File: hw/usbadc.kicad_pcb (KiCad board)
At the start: 4 copper layers, 100 x 60 mm, 253 parts, among them J1 Ext_Power, J10 BNC, J11 PEN_SEL, J12 PUDC_B/IN, J2 USB_C_Receptacle_USB2.0, J3 Jtag_Master, J4 JTAG, J5 GPIO2V5, J6 BNC, J7 BNC, J8 BNC, J9 Expansion, Q1 Si3477, Q2 Si3477, SW1 PROG_B, U1 TLV62569DDC, U10 LMH6882, U11 TSV992A, U12 OPA859xDSG, U13 OPA859xDSG, U14 MCP47CVB02-E_UN, U15 UTC2000, U16 74LVC1G32, U17 SN74LVC2T45DCUR, U2 TLV62569DDC, U3 TLV62569DDC, U4 FT240XS, U5 XC3S50A-VQ100, U6 AT25DF041B, U7 5P49V5925, U8 THS4522, U9 MAX19507, Y1 25MHz

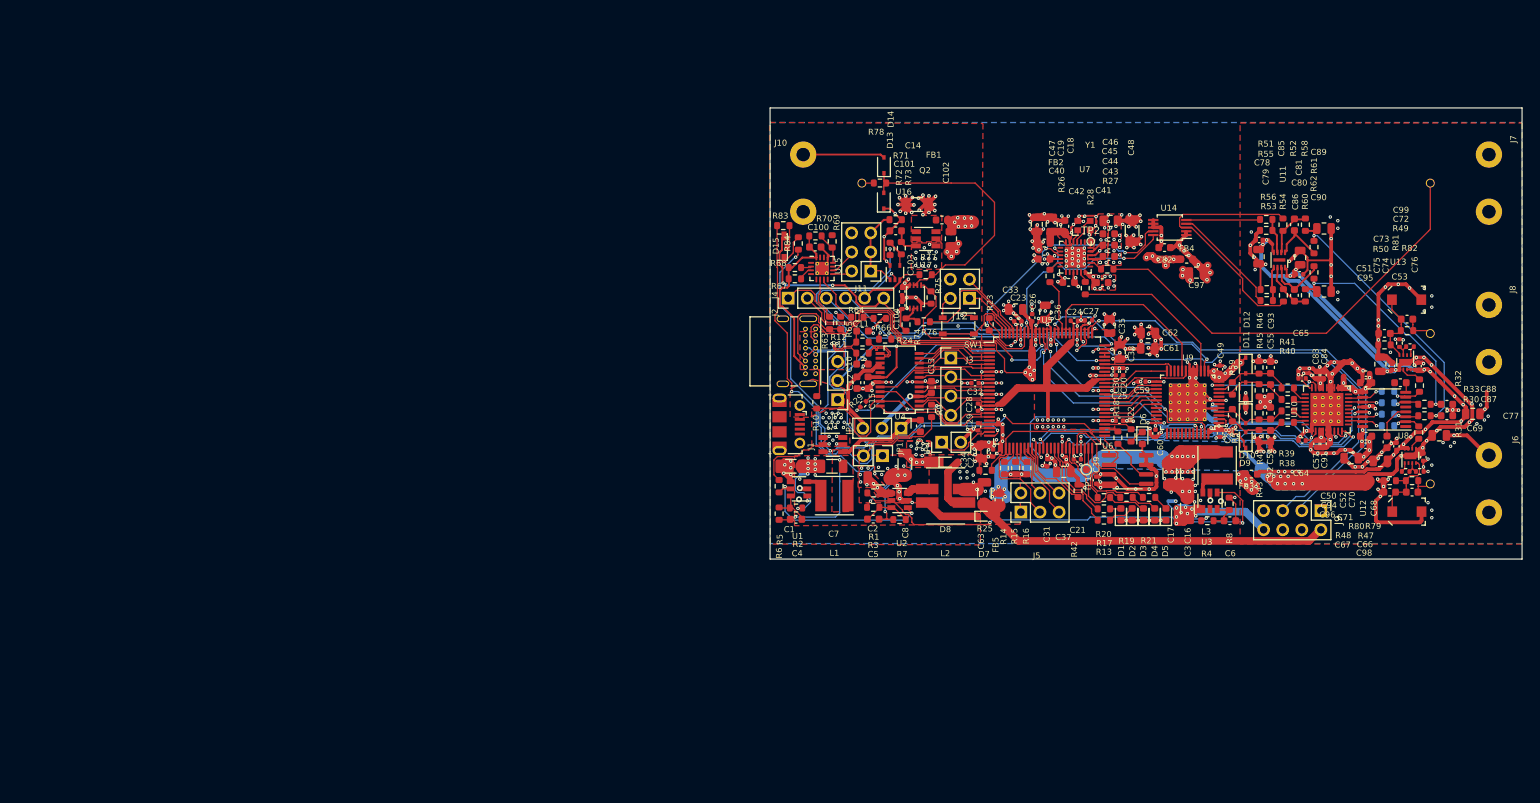
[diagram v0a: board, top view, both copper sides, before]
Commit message: basic schematic, started layout (placing first components)
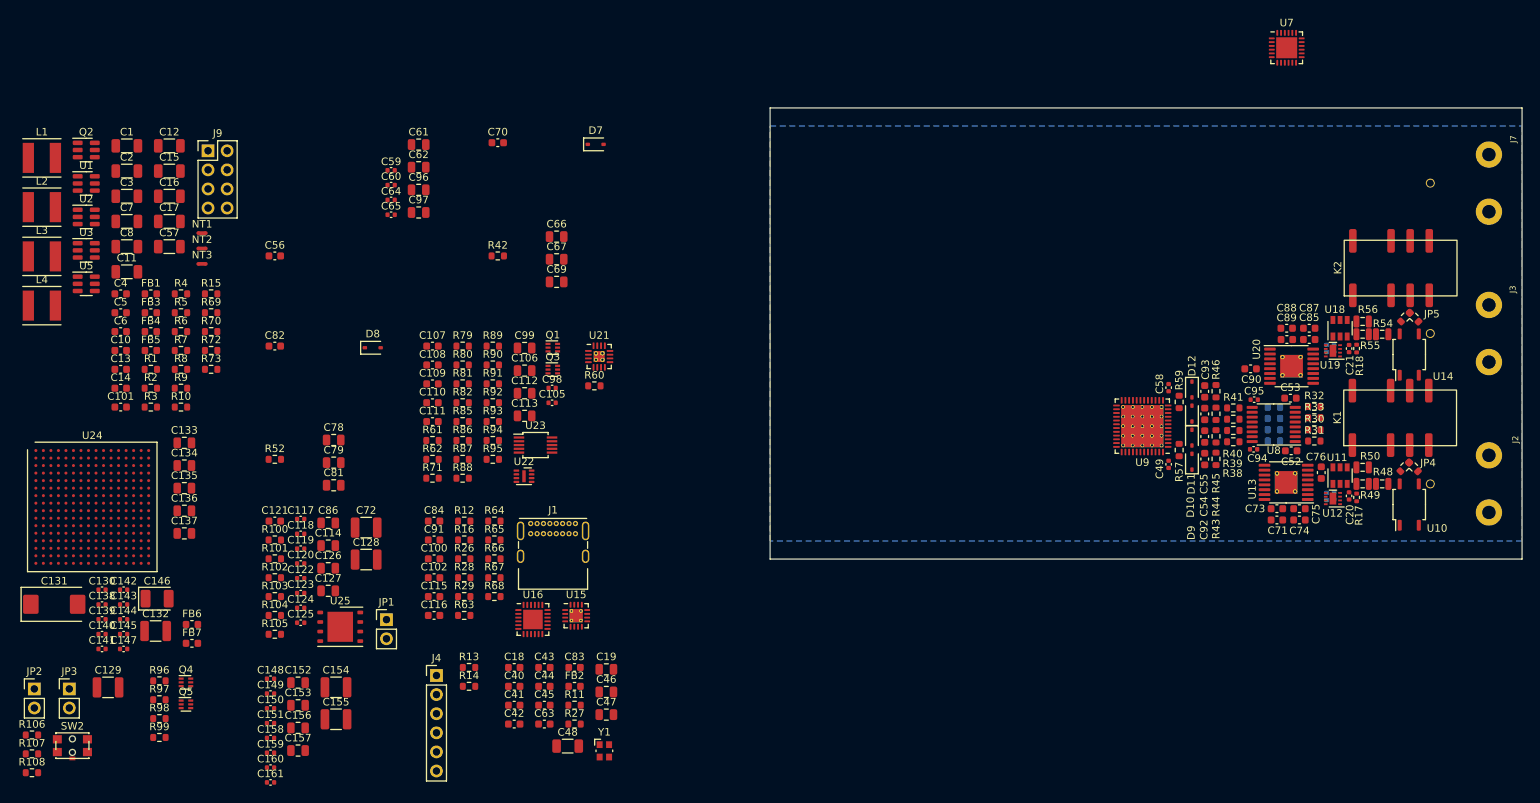
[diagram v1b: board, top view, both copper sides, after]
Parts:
- removed C103, C104, C22, C23, C24, C25, C26, C27, C28, C29, C30, C31, C32, C39: 100n, Capacitor_SMD:C_0402_1005Metric
- removed C33, C34, C35, C36, C37, C38: 1uF, Capacitor_SMD:C_0805_2012Metric
- removed C50, C51: 100n, Capacitor_SMD:C_0603_1608Metric
- removed D1, D2, D3, D4, D5, D6: LED, LED_SMD:LED_0603_1608Metric
- removed D13, D14: NSR0170HT1G, Diode_SMD:D_SOD-323
- removed D15: LED_Front, proj_footprints:LED_Wuerth_Sideview
- removed J10: BNC, proj_footprints:BNC_Molex_0731713150
- removed J11: PEN_SEL, Connector_PinHeader_2.54mm:PinHeader_2x03_P2.54mm_Vertical
- removed J12: PUDC_B/IN, Connector_PinHeader_2.54mm:PinHeader_2x02_P2.54mm_Vertical
- removed the J2 at (69.0, 52.4)
- removed the J3 at (87.0, 56.2)
- removed J5: GPIO2V5, Connector_PinHeader_2.54mm:PinHeader_2x03_P2.54mm_Vertical
- removed R19, R20, R21, R22, R83, R84: 1k5, Resistor_SMD:R_0603_1608Metric
- removed R23, R24, R25: 10k, Resistor_SMD:R_0603_1608Metric
- removed R47: 500k, Resistor_SMD:R_0603_1608Metric
- removed R51, R53, R58: 5k, Resistor_SMD:R_0603_1608Metric
- removed R74, R77: 100k, Resistor_SMD:R_0603_1608Metric
- removed R75: 2k2, Resistor_SMD:R_0603_1608Metric
- removed R76: 100, Resistor_SMD:R_0603_1608Metric
- removed R78: 50, Resistor_SMD:R_0603_1608Metric
- removed SW1: PROG_B, Button_Switch_SMD:SW_SPST_PTS810
- removed TP1: TP_INIT, TestPoint:TestPoint_Pad_D1.0mm
- removed TP2: Ref, proj_footprints:TestPoint_Pad_D0.8mm_no_CY
- removed U17: SN74LVC2T45DCUR, Package_SO:VSSOP-8_2.4x2.1mm_P0.5mm
- removed U4: FT240XS, Package_SO:SSOP-24_3.9x8.7mm_P0.635mm
- removed U6: AT25DF041B, Package_SO:SOIC-8_3.9x4.9mm_P1.27mm
- added C105: 100n, Capacitor_SMD:C_0402_1005Metric, F.Cu at (34.0, 62.2)
- added C106: 1u, Capacitor_SMD:C_0805_2012Metric, F.Cu at (30.3, 57.9)
- added C107: 100n, Capacitor_SMD:C_0603_1608Metric, F.Cu at (18.1, 54.7)
- added C108: 2n, Capacitor_SMD:C_0603_1608Metric, F.Cu at (18.1, 57.2)
- added C109: 2n, Capacitor_SMD:C_0603_1608Metric, F.Cu at (18.1, 59.7)
- added C110: 100n, Capacitor_SMD:C_0603_1608Metric, F.Cu at (18.1, 62.2)
- added C111: 100n, Capacitor_SMD:C_0603_1608Metric, F.Cu at (18.1, 64.7)
- added C112: 1u, Capacitor_SMD:C_0805_2012Metric, F.Cu at (30.3, 60.9)
- added C113: 1u, Capacitor_SMD:C_0805_2012Metric, F.Cu at (30.3, 64.0)
- added C114: 4u7, Capacitor_SMD:C_0805_2012Metric, F.Cu at (4.22, 81.2)
- added C115: 100n, Capacitor_SMD:C_0603_1608Metric, F.Cu at (18.3, 88.0)
- added C116: 100n, Capacitor_SMD:C_0603_1608Metric, F.Cu at (18.3, 90.5)
- added C117: 470n, Capacitor_SMD:C_0402_1005Metric, F.Cu at (0.56, 77.7)
- added C118: 470n, Capacitor_SMD:C_0402_1005Metric, F.Cu at (0.56, 79.6)
- added C119: 470n, Capacitor_SMD:C_0402_1005Metric, F.Cu at (0.56, 81.6)
- added C120: 470n, Capacitor_SMD:C_0402_1005Metric, F.Cu at (0.56, 83.6)
- added C121: 100n, Capacitor_SMD:C_0603_1608Metric, F.Cu at (-2.88, 77.9)
- added C122: 470n, Capacitor_SMD:C_0402_1005Metric, F.Cu at (0.56, 85.6)
- added C123: 470n, Capacitor_SMD:C_0402_1005Metric, F.Cu at (0.56, 87.5)
- added C124: 470n, Capacitor_SMD:C_0402_1005Metric, F.Cu at (0.56, 89.5)
- added C125: 470n, Capacitor_SMD:C_0402_1005Metric, F.Cu at (0.56, 91.5)
- added C126: 4u7, Capacitor_SMD:C_0805_2012Metric, F.Cu at (4.22, 84.2)
- added C127: 4u7, Capacitor_SMD:C_0805_2012Metric, F.Cu at (4.22, 87.2)
- added C128: 47u, Capacitor_SMD:C_1210_3225Metric, F.Cu at (9.28, 83.1)
- added C129: 47u, Capacitor_SMD:C_1210_3225Metric, F.Cu at (-25.1, 100.1)
- added C130: 470n, Capacitor_SMD:C_0402_1005Metric, F.Cu at (-25.9, 87.1)
- added C131: 330u, Capacitor_Tantalum_SMD:CP_EIA-7343-30_AVX-N, F.Cu at (-32.2, 89.0)
- added C132: 47u, Capacitor_SMD:C_1210_3225Metric, F.Cu at (-18.7, 92.6)
- added C133: 4u7, Capacitor_SMD:C_0805_2012Metric, F.Cu at (-14.9, 67.5)
- added C134: 4u7, Capacitor_SMD:C_0805_2012Metric, F.Cu at (-14.9, 70.6)
- added C135: 4u7, Capacitor_SMD:C_0805_2012Metric, F.Cu at (-14.9, 73.6)
- added C136: 4u7, Capacitor_SMD:C_0805_2012Metric, F.Cu at (-14.9, 76.6)
- added C137: 4u7, Capacitor_SMD:C_0805_2012Metric, F.Cu at (-14.9, 79.6)
- added C138: 470n, Capacitor_SMD:C_0402_1005Metric, F.Cu at (-25.9, 89.0)
- added C139: 470n, Capacitor_SMD:C_0402_1005Metric, F.Cu at (-25.9, 91.0)
- added C140: 470n, Capacitor_SMD:C_0402_1005Metric, F.Cu at (-25.9, 93.0)
- added C141: 470n, Capacitor_SMD:C_0402_1005Metric, F.Cu at (-25.9, 95.0)
- added C142: 470n, Capacitor_SMD:C_0402_1005Metric, F.Cu at (-23.0, 87.1)
- added C143: 470n, Capacitor_SMD:C_0402_1005Metric, F.Cu at (-23.0, 89.0)
- added C144: 470n, Capacitor_SMD:C_0402_1005Metric, F.Cu at (-23.0, 91.0)
- added C145: 470n, Capacitor_SMD:C_0402_1005Metric, F.Cu at (-23.0, 93.0)
- added C146: 100u, Capacitor_Tantalum_SMD:CP_EIA-3528-15_AVX-H, F.Cu at (-18.5, 88.3)
- added C147: 470n, Capacitor_SMD:C_0402_1005Metric, F.Cu at (-23.0, 95.0)
- added C148: 470n, Capacitor_SMD:C_0402_1005Metric, F.Cu at (-3.44, 98.9)
- added C149: 470n, Capacitor_SMD:C_0402_1005Metric, F.Cu at (-3.44, 100.9)
- added C150: 470n, Capacitor_SMD:C_0402_1005Metric, F.Cu at (-3.44, 102.9)
- added C151: 470n, Capacitor_SMD:C_0402_1005Metric, F.Cu at (-3.44, 104.8)
- added C152: 4u7, Capacitor_SMD:C_0805_2012Metric, F.Cu at (0.21, 99.4)
- added C153: 4u7, Capacitor_SMD:C_0805_2012Metric, F.Cu at (0.21, 102.4)
- added C154: 47u, Capacitor_SMD:C_1210_3225Metric, F.Cu at (5.26, 100.1)
- added C155: 47u, Capacitor_SMD:C_1210_3225Metric, F.Cu at (5.26, 104.3)
- added C156: 4u7, Capacitor_SMD:C_0805_2012Metric, F.Cu at (0.21, 105.5)
- added C157: 4u7, Capacitor_SMD:C_0805_2012Metric, F.Cu at (0.21, 108.5)
- added C158: 470n, Capacitor_SMD:C_0402_1005Metric, F.Cu at (-3.44, 106.8)
- added C159: 470n, Capacitor_SMD:C_0402_1005Metric, F.Cu at (-3.44, 108.8)
- added C160: 470n, Capacitor_SMD:C_0402_1005Metric, F.Cu at (-3.44, 110.7)
- added C161: 470n, Capacitor_SMD:C_0402_1005Metric, F.Cu at (-3.44, 112.7)
- added FB6: FB_250, Inductor_SMD:L_0603_1608Metric, F.Cu at (-13.9, 91.7)
- added FB7: FB_250, Inductor_SMD:L_0603_1608Metric, F.Cu at (-13.9, 94.2)
- added JP5: 50Ohm, proj_footprints:J_0603_V, F.Cu at (148.0, 50.3)
- added K1: G6S-2, proj_footprints:TX2SA, F.Cu at (140.4, 64.2)
- added K2: G6S-2, proj_footprints:TX2SA, F.Cu at (140.5, 44.3)
- added L4: 2u2, Inductor_SMD:L_Taiyo-Yuden_NR-50xx, F.Cu at (-33.9, 49.3)
- added Q3: SSM6N35AFE, proj_footprints:SOT-563-adjusted, F.Cu at (34.1, 57.8)
- added Q4: SSM6P35AFE, proj_footprints:SOT-563-adjusted, F.Cu at (-14.7, 99.4)
- added Q5: SSM6P35AFE, proj_footprints:SOT-563-adjusted, F.Cu at (-14.7, 102.3)
- added R100: 1k, Resistor_SMD:R_0603_1608Metric, F.Cu at (-2.88, 80.5)
- added R101: 100k, Resistor_SMD:R_0603_1608Metric, F.Cu at (-2.88, 83.0)
- added R102: 10k, Resistor_SMD:R_0603_1608Metric, F.Cu at (-2.88, 85.5)
- added R103: 10k, Resistor_SMD:R_0603_1608Metric, F.Cu at (-2.88, 88.0)
- added R104: 10k, Resistor_SMD:R_0603_1608Metric, F.Cu at (-2.88, 90.5)
- added R105: 50, Resistor_SMD:R_0603_1608Metric, F.Cu at (-2.88, 93.0)
- added R106: 1k, Resistor_SMD:R_0603_1608Metric, F.Cu at (-35.2, 106.4)
- added R107: 1k, Resistor_SMD:R_0603_1608Metric, F.Cu at (-35.2, 108.9)
- added R108: 1k, Resistor_SMD:R_0603_1608Metric, F.Cu at (-35.2, 111.4)
- added R85: 1k, Resistor_SMD:R_0603_1608Metric, F.Cu at (22.1, 64.7)
- added R86: 27k, Resistor_SMD:R_0603_1608Metric, F.Cu at (22.1, 67.2)
- added R87: 18k, Resistor_SMD:R_0603_1608Metric, F.Cu at (22.1, 69.7)
- added R88: 27k, Resistor_SMD:R_0603_1608Metric, F.Cu at (22.1, 72.2)
- added R89: 18k, Resistor_SMD:R_0603_1608Metric, F.Cu at (26.1, 54.7)
- added R90: 9k, Resistor_SMD:R_0603_1608Metric, F.Cu at (26.1, 57.2)
- added R91: 9k, Resistor_SMD:R_0603_1608Metric, F.Cu at (26.1, 59.7)
- added R92: 18k, Resistor_SMD:R_0603_1608Metric, F.Cu at (26.1, 62.2)
- added R93: 18k, Resistor_SMD:R_0603_1608Metric, F.Cu at (26.1, 64.7)
- added R94: 1, Resistor_SMD:R_0603_1608Metric, F.Cu at (26.1, 67.2)
- added R95: 1, Resistor_SMD:R_0603_1608Metric, F.Cu at (26.1, 69.7)
- added R96: 10k, Resistor_SMD:R_0603_1608Metric, F.Cu at (-18.2, 99.2)
- added R97: 10k, Resistor_SMD:R_0603_1608Metric, F.Cu at (-18.2, 101.7)
- added R98: 10k, Resistor_SMD:R_0603_1608Metric, F.Cu at (-18.2, 104.2)
- added R99: 10k, Resistor_SMD:R_0603_1608Metric, F.Cu at (-18.2, 106.7)
- added SW2: PROG, proj_footprints:SW_SPST_PTS810_and_PTS841, F.Cu at (-29.8, 107.8)
- added U18: TS5A63157DBV, proj_footprints:SOT-23-6_small_cyd, F.Cu at (138.8, 52.3)
- added U19: OPA859xDSG, Package_SON:WSON-8-1EP_2x2mm_P0.5mm_EP0.9x1.6mm, F.Cu at (137.8, 55.3)
- added U20: AD8370, Package_SO:TSSOP-16-1EP_4.4x5mm_P0.65mm_EP3x3mm_ThermalVias, F.Cu at (132.3, 57.4)
- added U21: TCA6408A, Package_DFN_QFN:QFN-16-1EP_3x3mm_P0.5mm_EP1.45x1.45mm_ThermalVias, F.Cu at (40.3, 56.1)
- added U22: TSV992A, proj_footprints:DFN-8-1EP_2x2mm_P0.5mm_EP0.45x1.6mm, F.Cu at (30.3, 72.0)
- added U23: MCP47CVB02-E_UN, Package_SO:MSOP-10_3x3mm_P0.5mm, F.Cu at (31.8, 67.8)
- added U24: XC7A35T-FTG256, Package_BGA:Xilinx_FTG256, F.Cu at (-27.2, 76.1)
- added U25: AT25SL641, Package_SON:WSON-8-1EP_6x5mm_P1.27mm_EP3.4x4mm, F.Cu at (5.83, 92.0)
- C10: value 47p -> 100n
- C100: value 100n -> 1u
- C102: value 1u -> 100n; footprint Capacitor_SMD:C_0805_2012Metric -> Capacitor_SMD:C_0603_1608Metric
- C11: value 47p -> 10u; footprint Capacitor_SMD:C_0603_1608Metric -> Capacitor_SMD:C_1206_3216Metric
- C12, C15: value 100n -> 10u; footprint Capacitor_SMD:C_0603_1608Metric -> Capacitor_SMD:C_1206_3216Metric
- C14: value 10u -> 50p; footprint Capacitor_SMD:C_1206_3216Metric -> Capacitor_SMD:C_0603_1608Metric
- C20, C21: value 100n -> 10p
- C56, NT1, NT2, NT3: moved to F.Cu
- C57: value 10n -> 10u; footprint Capacitor_SMD:C_0402_1005Metric -> Capacitor_SMD:C_1206_3216Metric
- C63: value 10u -> 100n; footprint Capacitor_SMD:C_1206_3216Metric -> Capacitor_SMD:C_0603_1608Metric
- C66: value 20p -> 100n; footprint Capacitor_SMD:C_0603_1608Metric -> Capacitor_SMD:C_0805_2012Metric
- C67: value 15p -> 1u; footprint Capacitor_SMD:C_0603_1608Metric -> Capacitor_SMD:C_0805_2012Metric
- C68, C80: moved to B.Cu
- C70: footprint Capacitor_SMD:C_0402_1005Metric -> Capacitor_SMD:C_0603_1608Metric
- C71: value 1u -> 100nF; footprint Capacitor_SMD:C_0805_2012Metric -> Capacitor_SMD:C_0603_1608Metric
- C72: value 20p -> 47u; footprint Capacitor_SMD:C_0603_1608Metric -> Capacitor_SMD:C_1210_3225Metric
- C73: value 15p -> 1n
- C74: value 100n -> 100nF; footprint Capacitor_SMD:C_0402_1005Metric -> Capacitor_SMD:C_0603_1608Metric
- C75, C89, C90: value 1u -> 1n; footprint Capacitor_SMD:C_0805_2012Metric -> Capacitor_SMD:C_0603_1608Metric
- C76: value 100n -> 1n; footprint Capacitor_SMD:C_0402_1005Metric -> Capacitor_SMD:C_0603_1608Metric
- C77: value 1u -> 100n; footprint Capacitor_SMD:C_0805_2012Metric -> Capacitor_SMD:C_0402_1005Metric; moved to B.Cu
- C78: footprint Capacitor_SMD:C_0402_1005Metric -> Capacitor_SMD:C_0805_2012Metric
- C83, C84: value 10n -> 100n; footprint Capacitor_SMD:C_0402_1005Metric -> Capacitor_SMD:C_0603_1608Metric
- C85: value 2n -> 100nF
- C86: value 2n -> 4u7; footprint Capacitor_SMD:C_0603_1608Metric -> Capacitor_SMD:C_0805_2012Metric
- C87: value 100n -> 1n
- C88: value 100n -> 100nF
- C9: footprint Capacitor_SMD:C_0603_1608Metric -> Capacitor_SMD:C_0402_1005Metric; moved to B.Cu
- C91: value 10n -> 1u; footprint Capacitor_SMD:C_0402_1005Metric -> Capacitor_SMD:C_0603_1608Metric
- C98: value 5-15p -> 100n; footprint proj_footprints:C_Trimmer_EW_Electronics_SCG3S -> Capacitor_SMD:C_0402_1005Metric
- C99: value 5-15p -> 1u; footprint proj_footprints:C_Trimmer_EW_Electronics_SCG3S -> Capacitor_SMD:C_0805_2012Metric
- D7: value CTS05S30 -> NSR0170HT1G; footprint proj_footprints:sod323 -> Diode_SMD:D_SOD-323
- D8: value CTS05S30 -> NSR0170HT1G; footprint proj_footprints:sod323-special -> Diode_SMD:D_SOD-323
- J1: value Ext_Power -> USB_C_Receptacle_USB2.0; footprint Connector_USB:USB_Micro-B_Molex-105017-0001 -> proj_footprints:USB_C_Receptacle_GCT_USB4085_smaller_holes
- JP1: value Jumper_2_Open -> PUDC_dis
- JP2: value Jumper_ExtSup -> JTAG_boot; footprint Connector_PinHeader_2.54mm:PinHeader_1x03_P2.54mm_Vertical -> Connector_PinHeader_2.54mm:PinHeader_1x02_P2.54mm_Vertical
- JP3: value Jumper_JTAG_hack -> INITb; footprint Connector_PinHeader_2.54mm:PinHeader_1x03_P2.54mm_Vertical -> Connector_PinHeader_2.54mm:PinHeader_1x02_P2.54mm_Vertical
- JP4: value Mode_JTAG -> 50Ohm; footprint Connector_PinHeader_2.54mm:PinHeader_1x02_P2.54mm_Vertical -> proj_footprints:J_0603_V
- L2: value 2.2u -> 2u2; footprint proj_footprints:L_Taiyo-Yuden_NR-50xx+bourns0703 -> Inductor_SMD:L_Taiyo-Yuden_NR-50xx
- Q1: value Si3477 -> SSM6N35AFE; footprint Package_TO_SOT_SMD:TSOT-23-6 -> proj_footprints:SOT-563-adjusted
- R10: value 47k -> 10k
- R11, R12: value 27 -> 10k
- R13: value 1k5 -> 10k
- R14, R16: value 0 -> 10k
- R15: value 0 -> 100k
- R17: value 1k5 -> 1M; footprint Resistor_SMD:R_0603_1608Metric -> Resistor_SMD:R_0402_1005Metric
- R18: value 50 -> 1M; footprint Resistor_SMD:R_0603_1608Metric -> Resistor_SMD:R_0402_1005Metric
- R26: value 33 -> 10k
- R28: value 33 -> 5k1
- R29: value 50 -> 5k1; footprint Resistor_SMD:R_0402_1005Metric -> Resistor_SMD:R_0603_1608Metric
- R3: value 100k -> 10k
- R4: value 100k -> 27k
- R42: value 250 -> 1k2
- R48, R49: value 500k -> 909k/11p; footprint Resistor_SMD:R_0603_1608Metric -> proj_footprints:RC_0603_1608Metric
- R50: value 500k -> 100k/100p; footprint Resistor_SMD:R_0603_1608Metric -> proj_footprints:RC_0603_1608Metric
- R52: value 10k -> 1k2
- R54, R55: value 10k -> 909k/11p; footprint Resistor_SMD:R_0603_1608Metric -> proj_footprints:RC_0603_1608Metric
- R56: value 10k -> 100k/100p; footprint Resistor_SMD:R_0603_1608Metric -> proj_footprints:RC_0603_1608Metric
- R60: value 5k -> 10k
- R61, R62: value 1 -> 18k
- R66: value 5k1 -> 35k7
- R67: value 10k -> 8.06k
- R69: value 5k1 -> 0
- R7: value 316k -> 31k6
- R70: value 35k7 -> 0
- R71, R8: value 100k -> 18k
- R72: value 100k -> 0
- R79: value 150 -> 18k; footprint Resistor_SMD:R_0402_1005Metric -> Resistor_SMD:R_0603_1608Metric
- R80, R82: value 750 -> 1k; footprint Resistor_SMD:R_0402_1005Metric -> Resistor_SMD:R_0603_1608Metric
- R81: value 150 -> 1k; footprint Resistor_SMD:R_0402_1005Metric -> Resistor_SMD:R_0603_1608Metric
- R9: value 100k -> 31k6
- U10: value LMH6882 -> CPC1017N; footprint Package_DFN_QFN:Texas_S-PVQFN-N36_EP4.4x4.4mm_ThermalVias -> Package_SO:SOP-4_3.8x4.1mm_P2.54mm
- U11: value TSV992A -> TS5A63157DBV; footprint proj_footprints:DFN-8-1EP_2x2mm_P0.5mm_EP0.45x1.6mm -> proj_footprints:SOT-23-6_small_cyd
- U13: value OPA859xDSG -> AD8370; footprint Package_SON:WSON-8-1EP_2x2mm_P0.5mm_EP0.9x1.6mm -> Package_SO:TSSOP-16-1EP_4.4x5mm_P0.65mm_EP3x3mm_ThermalVias
- U14: value MCP47CVB02-E_UN -> CPC1017N; footprint Package_SO:MSOP-10_3x3mm_P0.5mm -> Package_SO:SOP-4_3.8x4.1mm_P2.54mm
- U16: value 74LVC1G32 -> USB3343; footprint Package_TO_SOT_SMD:SOT-353_SC-70-5 -> Package_DFN_QFN:QFN-24-1EP_4x4mm_P0.5mm_EP2.6x2.6mm
- U5: value XC3S50A-VQ100 -> TPS563249DDC; footprint Package_QFP:VQFP-100_14x14mm_P0.5mm -> Package_TO_SOT_SMD:SOT-23-6
- U9: value MAX19507 -> MAX19517; footprint Package_QFP:TQFP-48-1EP_7x7mm_P0.5mm_EP5x5mm_ThermalVias -> proj_footprints:QFN-48-1EP_7x7mm_P0.5mm_EP5.6x5.6mm_ThermalVias_biggerholes
- Y1: value 25MHz -> 26MHz
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- renumbered J6 to J2, J8 to J3
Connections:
- net /pll_clock/CLK_OUT renamed /Clock/CLK_OUT
- C10 pad 2: /Power/USBin_P -> +5V
- C100 pad 1: VBUS -> GND
- C100 pad 2: GND -> Net-(U16-ID)
- C102 pad 1: Vpp_analog -> +5V
- C11 pad 1: /Power/USBin_N -> GND
- C11 pad 2: GND -> +5V
- C12 pad 1: GND -> Net-(U5-GND)
- C12 pad 2: Net-(C12-Pad2) -> +5V
- C13 pad 1: GND -> Net-(U5-SW)
- C13 pad 2: Net-(C13-Pad2) -> Net-(U5-VBST)
- C14 pad 1: +5V -> GND
- C14 pad 2: GND -> Net-(U5-VFB)
- C15 pad 2: +5V -> Net-(U5-GND)
- C16 pad 1: +1V2 -> Net-(C16-Pad1)
- C17 pad 1: +1V2 -> Net-(C16-Pad1)
- C20 pad 1: +1V2 -> Net-(U11-NC)
- C20 pad 2: GND -> Net-(U12-FB)
- C21 pad 1: +2V5 -> Net-(U18-NC)
- C21 pad 2: GND -> Net-(U19-FB)
- C4 pad 1: +1V8_perm -> Net-(C4-Pad1)
- C5 pad 1: +2V5 -> Net-(C5-Pad1)
- C52 pad 2: Net-(C52-Pad2) -> Net-(U8A-VOCM2)
- C53 pad 2: Net-(C53-Pad2) -> Net-(U8B-VOCM2)
- C57 pad 1: Vpp_analog -> GND
- C57 pad 2: GND -> Net-(U5-GND)
- C6 pad 1: +1V2 -> Net-(C16-Pad1)
- C63 pad 1: /Power/-2V5_dig -> /ADC+Driver/ADC_CLK_P
- C63 pad 2: GND -> Net-(U7-OUT4)
- C64 pad 2: Net-(C64-Pad2) -> Net-(U8A-VOCM2)
- C65 pad 1: Net-(C65-Pad1) -> Net-(U8B-VOCM2)
- C66 pad 1: Net-(C66-Pad1) -> Net-(JP4-B)
- C66 pad 2: Net-(C66-Pad2) -> Net-(J2-In)
- C67 pad 1: GND -> -2V5_analog
- C67 pad 2: Net-(C66-Pad2) -> GND
- C68 pad 1: -2V5 -> +2V5_analog
- C69 pad 1: -2V5 -> +2V5_analog
- C7 pad 1: +1V8_perm -> Net-(C4-Pad1)
- C70 pad 1: +2V5_analog -> GND
- C70 pad 2: GND -> +5V
- C71 pad 1: +2V5_analog -> -2V5_analog
- C72 pad 1: Net-(C72-Pad1) -> +1V8
- C72 pad 2: Net-(C72-Pad2) -> GND
- C73 pad 1: GND -> -2V5_analog
- C73 pad 2: Net-(C72-Pad2) -> GND
- C74 pad 1: -2V5 -> +2V5_analog
- C75 pad 1: -2V5 -> +2V5_analog
- C76 pad 1: +2V5_analog -> Net-(U13-VOCM)
- C77 pad 1: +2V5_analog -> -2V5_analog
- C78 pad 1: -2V5 -> Net-(JP5-B)
- C78 pad 2: GND -> Net-(J3-In)
- C79 pad 1: -2V5 -> -2V5_analog
- C8 pad 1: +2V5 -> Net-(C5-Pad1)
- C82 pad 2: +1V8_analog -> +5V
- C83 pad 1: Vpp_analog -> /ADC+Driver/ADC_CLK_N
- C83 pad 2: GND -> Net-(U7-OUT4B)
- C84 pad 1: Vpp_analog -> +5V
- C85 pad 1: Net-(C85-Pad1) -> -2V5_analog
- C85 pad 2: Net-(C85-Pad2) -> GND
- C86 pad 1: Net-(C86-Pad1) -> +1V8
- C86 pad 2: Net-(C86-Pad2) -> GND
- C87 pad 1: GND -> -2V5_analog
- C87 pad 2: /ADC+Driver/offset_dac/DAC_0 -> GND
- C88 pad 1: GND -> +2V5_analog
- C88 pad 2: /ADC+Driver/offset_dac/DAC_1 -> GND
- C89 pad 1: /ADC+Driver/offset_dac/DAC_0 -> +2V5_analog
- C9 pad 1: Net-(C9-Pad1) -> -2V5_analog
- C9 pad 2: +1V8_perm -> GND
- C90 pad 1: /ADC+Driver/offset_dac/DAC_1 -> Net-(U20-VOCM)
- C91 pad 1: Vpp_analog -> GND
- C91 pad 2: GND -> Net-(U16-VDD18)
- C98 pad 1: Net-(C66-Pad2) -> -2V5_analog
- C99 pad 1: Net-(C72-Pad2) -> -2V5_analog
- D7 pad 1: Net-(D7-Pad1) -> /Front End/FE_CHA/FE_CTL_TERM
- D7 pad 2: /Power/-2V5_dig -> GND
- D8 pad 1: +2V5 -> /Front End/FE_CHB/FE_CTL_TERM
- D8 pad 2: Net-(D8-Pad2) -> GND
- FB5 pad 1: /Power/-2V5_dig -> Net-(U5-GND)
- FB5 pad 2: -2V5 -> -2V5_analog
- J2 pad 1: Net-(C66-Pad1) -> Net-(J2-In)
- J3 pad 1: Net-(C72-Pad1) -> Net-(J3-In)
- J4 pad 1: /fpga_xc3s/TMS -> TMS
- J4 pad 2: /fpga_xc3s/TDI -> TDI
- J4 pad 3: /fpga_xc3s/TDO -> TDO
- J4 pad 4: /fpga_xc3s/TCK -> TCK
- J4 pad 6: +2V5 -> +1V8
- J9 pad 2: /Power/-2V5_dig -> -2V5_analog
- J9 pad 3: EXP_IO1_1V8 -> IO_L19P_T3_35
- J9 pad 5: EXP_IO2_1V8 -> IO_L19N_T3_VREF_35
- JP1 pad 1: GND -> +1V8
- JP1 pad 2: Net-(JP1-Pad2) -> Net-(U24A-IO_L3P_T0_DQS_PUDC_B_14)
- JP2 pad 1: Net-(J1-Pad1) -> +1V8
- JP2 pad 2: +5V -> Net-(U24C-M2_0)
- JP3 pad 1: +1V8_perm -> Net-(U24C-INIT_B_0)
- JP3 pad 2: Net-(C13-Pad2) -> GND
- JP4 pad 1: Net-(JP4-Pad1) -> Net-(J2-In)
- JP4 pad 2: GND -> Net-(JP4-C)
- L1 pad 1: +1V8_perm -> Net-(C4-Pad1)
- L2 pad 1: Net-(D7-Pad1) -> Net-(C5-Pad1)
- L3 pad 1: +1V2 -> Net-(C16-Pad1)
- Q1 pad 1: +1V8 -> GND
- Q1 pad 2: +1V8 -> IO_L23N_T3_35
- Q1 pad 3: Net-(C9-Pad1) -> Net-(Q1B-D)
- Q1 pad 4: +1V8_perm -> GND
- Q1 pad 5: +1V8 -> IO_L23N_T3_35
- Q1 pad 6: +1V8 -> Net-(Q1A-D)
- R1 pad 2: Net-(R1-Pad2) -> Net-(U1-EN)
- R10 pad 1: VBUS -> Net-(U5-GND)
- R10 pad 2: Net-(R10-Pad2) -> Net-(U5-VFB)
- R11 pad 1: /Power/USBin_P -> GND
- R11 pad 2: /Power/USBD_P -> /Clock/USB_REF_CLK
- R12 pad 1: /Power/USBin_N -> Net-(J1-CC2)
- R12 pad 2: /Power/USBD_N -> Net-(U15-CC2)
- R13 pad 1: Net-(R13-Pad1) -> IO_L20N_T3_35
- R13 pad 2: Net-(D2-Pad2) -> +1V8
- R14 pad 1: Net-(R14-Pad1) -> IO_L20P_T3_35
- R14 pad 2: GND -> +1V8
- R15 pad 1: Net-(R15-Pad1) -> /Power/PG_2V5
- R15 pad 2: GND -> +5V
- R16 pad 1: Net-(R16-Pad1) -> +1V8
- R16 pad 2: GND -> IO_L19P_T3_A10_D26_14
- R17 pad 1: Net-(R17-Pad1) -> Net-(U12-FB)
- R17 pad 2: Net-(D1-Pad2) -> Net-(U11-NC)
- R18 pad 1: Net-(R18-Pad1) -> Net-(U19-FB)
- R18 pad 2: Net-(R18-Pad2) -> Net-(U18-NC)
- R26 pad 1: FPGA_CLK -> Net-(J1-CC1)
- R26 pad 2: Net-(R26-Pad2) -> Net-(U15-CC1)
- R27 pad 2: Net-(R27-Pad2) -> Net-(U7-OUT3)
- R28 pad 1: ADC_CLK -> Net-(J1-CC2)
- R28 pad 2: Net-(R28-Pad2) -> GND
- R29 pad 1: Net-(R29-Pad1) -> Net-(J1-CC1)
- R29 pad 2: FIFO_CLK -> GND
- R30 pad 2: /ADC+Driver/offset_dac/DAC_0 -> /ADC+Driver/ADC_CHA_IN_P
- R31 pad 2: /ADC+Driver/buffer/OUT -> /ADC+Driver/ADC_CHA_IN_N
- R32 pad 2: /ADC+Driver/sheet611E90A8/OUT -> /ADC+Driver/ADC_CHB_IN_P
- R33 pad 2: /ADC+Driver/offset_dac/DAC_1 -> /ADC+Driver/ADC_CHB_IN_N
- R38 pad 2: Net-(R38-Pad2) -> /ADC+Driver/PGA_INA_N
- R39 pad 2: Net-(R39-Pad2) -> /ADC+Driver/PGA_INA_P
- R40 pad 2: Net-(R40-Pad2) -> /ADC+Driver/PGA_INB_N
- R41 pad 2: Net-(R41-Pad2) -> /ADC+Driver/PGA_INB_P
- R42 pad 1: PGA_SDO -> Net-(R42-Pad1)
- R42 pad 2: GND -> /Front End/FE_CHA/FE_CTL_AC
- R48 pad 1: GND -> Net-(R48-Pad1)
- R48 pad 2: Net-(C66-Pad2) -> Net-(JP4-B)
- R49 pad 1: Net-(C72-Pad2) -> Net-(U11-NC)
- R49 pad 2: Net-(C72-Pad1) -> Net-(R48-Pad1)
- R5 pad 1: Net-(R5-Pad1) -> Net-(U1-PG)
- R5 pad 2: +1V8 -> +5V
- R50 pad 1: GND -> Net-(U11-COM)
- R50 pad 2: Net-(C72-Pad2) -> Net-(R48-Pad1)
- R52 pad 2: Net-(C85-Pad2) -> /Front End/FE_CHB/FE_CTL_AC
- R54 pad 1: Net-(R52-Pad1) -> Net-(R54-Pad1)
- R54 pad 2: Net-(C86-Pad2) -> Net-(JP5-B)
- R55 pad 1: GND -> Net-(U18-NC)
- R55 pad 2: Net-(R51-Pad2) -> Net-(R54-Pad1)
- R56 pad 1: GND -> Net-(U18-COM)
- R56 pad 2: Net-(R53-Pad2) -> Net-(R54-Pad1)
- R6 pad 1: +1V8_perm -> Net-(C4-Pad1)
- R60 pad 1: /ADC+Driver/offset_dac/DAC_1 -> Net-(U21-RESETb)
- R60 pad 2: Net-(C86-Pad2) -> +1V8_analog
- R61 pad 1: /ADC+Driver/offset_dac/DAC_0 -> Net-(U23-VREF)
- R61 pad 2: Net-(C85-Pad1) -> Net-(R61-Pad2)
- R62 pad 1: /ADC+Driver/offset_dac/DAC_1 -> Net-(U23-VOUT1)
- R62 pad 2: Net-(C86-Pad1) -> Net-(R62-Pad2)
- R63 pad 1: Net-(J2-PadB5) -> +5V
- R63 pad 2: Net-(R63-Pad2) -> Net-(U15-Enable)
- R64 pad 1: Net-(J2-PadA5) -> +5V
- R64 pad 2: Net-(R64-Pad2) -> Net-(U15-CFG_SEL)
- R65 pad 1: Net-(J2-PadB5) -> Net-(U15-VMON)
- R66 pad 1: Net-(J2-PadA5) -> +5V
- R66 pad 2: GND -> Net-(U15-VMON)
- R67 pad 1: VBUS -> Net-(U16-RBIAS)
- R67 pad 2: Net-(R67-Pad2) -> GND
- R68 pad 1: VBUS -> +5V
- R68 pad 2: Net-(R68-Pad2) -> Net-(U16-VBUS)
- R69 pad 1: Net-(R69-Pad1) -> Net-(C4-Pad1)
- R69 pad 2: GND -> +1V8
- R7 pad 1: +2V5 -> Net-(C5-Pad1)
- R70 pad 1: VBUS -> Net-(C5-Pad1)
- R70 pad 2: Net-(R69-Pad1) -> +2V5
- R71 pad 1: Net-(J11-Pad1) -> Net-(U23-VREF)
- R71 pad 2: +5V -> Net-(R71-Pad2)
- R72 pad 1: Net-(C9-Pad1) -> Net-(C16-Pad1)
- R72 pad 2: /Power/PWR_EN -> +1V0
- R79 pad 1: Net-(R79-Pad1) -> Net-(U23-VOUT0)
- R79 pad 2: GND -> Net-(R79-Pad2)
- R8 pad 2: +1V2 -> Net-(C16-Pad1)
- R80 pad 1: Net-(R80-Pad1) -> Net-(Q1A-D)
- R80 pad 2: Net-(R79-Pad1) -> Net-(R61-Pad2)
- R81 pad 1: Net-(R81-Pad1) -> Net-(Q1B-D)
- R81 pad 2: GND -> Net-(R62-Pad2)
- R82 pad 1: Net-(R82-Pad1) -> Net-(Q3A-D)
- R82 pad 2: Net-(R81-Pad1) -> Net-(R71-Pad2)
- R9 pad 1: Net-(JP1-Pad2) -> Net-(U5-VFB)
- R9 pad 2: Net-(R10-Pad2) -> GND
- U1 pad 1: +5V -> Net-(U1-EN)
- U1 pad 5: Net-(R5-Pad1) -> Net-(U1-PG)
- U10 pad 1: GND -> Net-(R42-Pad1)
- U10 pad 2: Net-(C64-Pad2) -> GND
- U10 pad 3: Vpp_analog -> Net-(J2-In)
- U10 pad 4: Vpp_analog -> Net-(JP4-B)
- U11 pad 1: Net-(C85-Pad1) -> GND
- U11 pad 2: Net-(C85-Pad2) -> GND
- U11 pad 3: Net-(R51-Pad2) -> Net-(U11-NC)
- U11 pad 4: -2V5 -> Net-(U11-COM)
- U11 pad 5: Net-(R53-Pad2) -> +5V
- U11 pad 6: Net-(C86-Pad2) -> /Front End/FE_CHA/FE_CTL_ATT
- U12 pad 1: Net-(R80-Pad1) -> Net-(U12-FB)
- U12 pad 2: Net-(U12-Pad2) -> unconnected-(U12-NC-Pad2)
- U12 pad 3: Net-(R79-Pad1) -> Net-(U11-NC)
- U12 pad 4: Net-(C66-Pad2) -> GND
- U12 pad 5: -2V5 -> -2V5_analog
- U12 pad 6: /ADC+Driver/buffer/OUT -> Net-(U13-INLO)
- U12 pad 9: -2V5 -> -2V5_analog
- U13 pad 1: Net-(R82-Pad1) -> /Front End/FE_CHA/PGA_INHI
- U13 pad 2: Net-(U13-Pad2) -> -2V5_analog
- U13 pad 3: Net-(R81-Pad1) -> +2V5_analog
- U13 pad 4: Net-(C72-Pad2) -> +2V5_analog
- U13 pad 5: -2V5 -> Net-(U13-VOCM)
- U13 pad 6: /ADC+Driver/sheet611E90A8/OUT -> +2V5_analog
- U13 pad 7: +2V5_analog -> -2V5_analog
- U13 pad 8: +2V5_analog -> /ADC+Driver/ADC_CHA_IN_N
- U13 pad 9: -2V5 -> /ADC+Driver/ADC_CHA_IN_P
- U14 pad 1: +1V8_analog -> Net-(R52-Pad1)
- U14 pad 2: +1V8_analog -> GND
- U14 pad 3: Net-(R52-Pad1) -> Net-(J3-In)
- U14 pad 4: Net-(R53-Pad1) -> Net-(JP5-B)
- U15 pad 1: Net-(U15-Pad1) -> unconnected-(U15-OCS#-Pad1)
- U15 pad 10: /Power/3A0 -> /USB/3A0
- U15 pad 11: Net-(U15-Pad11) -> unconnected-(U15-Orient#-Pad11)
- U15 pad 12: Net-(R69-Pad1) -> Net-(U15-VMON)
- U15 pad 14: Net-(U15-Pad14) -> unconnected-(U15-NC-Pad14)
- U15 pad 15: Net-(U15-Pad15) -> unconnected-(U15-NC-Pad15)
- U15 pad 16: VBUS -> +5V
- U15 pad 2: Net-(R68-Pad2) -> Net-(U15-CFG_SEL)
- U15 pad 3: Net-(R67-Pad2) -> Net-(U15-Enable)
- U15 pad 4: Net-(U15-Pad4) -> unconnected-(U15-Fault_Ind-Pad4)
- U15 pad 5: Net-(U15-Pad5) -> unconnected-(U15-CONN#-Pad5)
- U15 pad 6: Net-(R63-Pad2) -> Net-(U15-CC2)
- U15 pad 7: Net-(R64-Pad2) -> Net-(U15-CC1)
- U15 pad 8: Net-(U15-Pad8) -> unconnected-(U15-LEG#-Pad8)
- U15 pad 9: /Power/1A5 -> /USB/1A5
- U16 pad 1: Net-(J11-Pad1) -> IO_L14P_T2_SRCC_14
- U16 pad 2: Net-(JP1-Pad2) -> IO_L13P_T2_MRCC_14
- U16 pad 3: GND -> IO_L13N_T2_MRCC_14
- U16 pad 4: /Power/PWR_EN -> IO_L15P_T2_DQS_RDWR_B_14
- U16 pad 5: +5V -> IO_L15N_T2_DQS_DOUT_CSO_B_14
- U2 pad 1: Net-(R5-Pad1) -> Net-(U1-PG)
- U2 pad 5: Net-(R1-Pad2) -> /Power/PG_2V5
- U3 pad 1: Net-(R1-Pad2) -> +5V
- U3 pad 5: Net-(U3-Pad5) -> Net-(U1-EN)
- U5 pad 1: /fpga_xc3s/TMS -> Net-(U5-GND)
- U5 pad 2: /fpga_xc3s/TDI -> Net-(U5-SW)
- U5 pad 3: FIFO_WRb -> +5V
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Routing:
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- removed copper zone on F.Cu, net +1V2
- removed copper zone on In2.Cu, net +1V2
- removed copper zone on F.Cu, net +1V8
- removed copper zone on In2.Cu, net +1V8
- removed copper zone on In2.Cu, net +1V8_analog
- removed copper zone on F.Cu, net +1V8_perm
- removed copper zone on F.Cu, net +2V5
- removed copper zone on In2.Cu, net +2V5
- removed copper zone on F.Cu, net +5V
- removed copper zone on In2.Cu, net +5V
- removed copper zone on B.Cu, net -2V5
- removed copper zone on F.Cu, net GND
- removed copper zone on In2.Cu, net GND
- removed copper zone on F.Cu, net Net-(FB1-Pad1)
- removed copper zone on F.Cu, net Net-(J1-Pad1)
- removed copper zone on F.Cu, net Net-(U7-VDDA)
- removed copper zone on F.Cu, net VBUS
- removed copper zone on In2.Cu, net VBUS
- removed copper zone on In2.Cu, net Vpp_analog
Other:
- net class 50OhmLine removed
- net class Default removed
- net class clr3p5 removed
- board text removed: "USBFastADC V1.0.0"

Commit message: WIP (layout)
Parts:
- removed C157: 4u7, Capacitor_SMD:C_0805_2012Metric
- removed C158: 470n, Capacitor_SMD:C_0402_1005Metric
- removed R105: 50, Resistor_SMD:R_0603_1608Metric
- added C22: 100n, Capacitor_SMD:C_0402_1005Metric, F.Cu at (59.4, 110.6)
- added C23: 100n, Capacitor_SMD:C_0402_1005Metric, F.Cu at (59.4, 112.5)
- added D1: NSR0170HT1G, Diode_SMD:D_SOD-323, F.Cu at (66.8, 109.5)
- added D2: NSR0170HT1G, Diode_SMD:D_SOD-323, F.Cu at (66.8, 112.5)
- added J5: BNC, proj_footprints:BNC_Molex_0731713150, F.Cu at (63.0, 72.2)
- added R19: 100, Resistor_SMD:R_0603_1608Metric, F.Cu at (66.7, 96.8)
- added R20: 100k, Resistor_SMD:R_0603_1608Metric, F.Cu at (66.7, 99.3)
- added R21: 2k2, Resistor_SMD:R_0603_1608Metric, F.Cu at (66.7, 101.8)
- added R22: 100k, Resistor_SMD:R_0603_1608Metric, F.Cu at (66.7, 104.3)
- added R23: 50, Resistor_SMD:R_0603_1608Metric, F.Cu at (66.7, 106.8)
- added U4: SN74LVC2T45DCUR, Package_SO:VSSOP-8_2.4x2.1mm_P0.5mm, F.Cu at (75.8, 75.5)
- C114, C117, C118, C119, C120, C122, C123, C124, C125, C126, C127, C130, C133, C134, C135, C136, C137, C138, C139, C140, C141, C142, C143, C144, C145, C148, C149, C150, C151, C152, C153, C156, C159, C160, C161, C86, FB6, FB7: moved to B.Cu
- moved C140 127.2 mm to (97.4, 61.6), turned to 90 degrees
- moved C138 126.1 mm to (96.9, 60.2), turned to 180 degrees
- moved C139 125.7 mm to (95.5, 58.0), turned to 180 degrees
- moved C141 123.5 mm to (93.4, 63.0), turned to 180 degrees
- moved U24 122.9 mm to (94.9, 61.5)
- moved C130 122.7 mm to (93.9, 60.5), turned to -90 degrees
- moved C143 121.8 mm to (95.8, 62.1)
- moved C142 121.7 mm to (96.5, 63.7), turned to -90 degrees
- moved L4 121.5 mm to (87.3, 41.0), turned to 90 degrees
- moved C145 119.7 mm to (91.8, 59.1), turned to 180 degrees
- moved C144 118.5 mm to (91.9, 62.0), turned to 180 degrees
- moved C133 114.8 mm to (99.7, 59.5)
- moved L3 114.7 mm to (80.8, 41.0), turned to 90 degrees
- moved C136 114.5 mm to (98.9, 64.0)
- moved C135 114.3 mm to (98.1, 56.5)
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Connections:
- U25 pad 2: Net-(U25-SO/SIO1) -> Net-(U24A-IO_L1N_T0_D01_DIN_14)
- U9 pad 14: IO_L11P_T1_SRCC_35 -> IO_L10N_T1_AD11N_15
- U9 pad 19: IO_L11N_T1_SRCC_35 -> IO_L10P_T1_AD11P_15
- U9 pad 20: IO_L12P_T1_MRCC_35 -> IO_L12P_T1_MRCC_15
- U9 pad 21: IO_L12N_T1_MRCC_35 -> IO_L17N_T2_A25_15
- U9 pad 22: IO_L13P_T2_MRCC_35 -> IO_L15N_T2_DQS_ADV_B_15
- U9 pad 23: IO_L13N_T2_MRCC_35 -> IO_L18N_T2_A23_15
- U9 pad 24: IO_L14P_T2_SRCC_35 -> IO_L21N_T3_DQS_A18_15
- U9 pad 26: IO_L14N_T2_SRCC_35 -> IO_L18P_T2_A24_15
- U9 pad 27: IO_L15P_T2_DQS_35 -> IO_L21P_T3_DQS_15
- U9 pad 28: IO_L15N_T2_DQS_35 -> IO_L24N_T3_RS0_15
- U9 pad 29: IO_L16P_T2_35 -> IO_L23P_T3_FOE_B_15
- U9 pad 30: IO_L16N_T2_35 -> IO_L22P_T3_A17_15
- U9 pad 31: IO_L17P_T2_35 -> IO_L23N_T3_FWE_B_15
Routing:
- net GND: track 1.24 -> 99.4 mm, vias 0 -> 39
- net +1V8: track 0.00 -> 85.7 mm, vias 0 -> 28
- net Net-(U24A-IO_L6P_T0_FCS_B_14): track 0.00 -> 22.1 mm
- net +1V0: track 0.00 -> 21.4 mm, vias 0 -> 9
- net /FPGA A7/bank14_15/CCLK: track 0.00 -> 18.4 mm
- net Net-(U24C-PROGRAM_B_0): track 0.00 -> 15.1 mm
- net IO_L12P_T1_MRCC_15: track 0.00 -> 14.9 mm
- net Net-(U24A-IO_L1N_T0_D01_DIN_14): track 0.00 -> 13.9 mm
- net Net-(U24A-IO_L1P_T0_D00_MOSI_14): track 0.00 -> 13.0 mm
- net IO_L10P_T1_AD11P_15: track 0.00 -> 12.7 mm
- net IO_L15N_T2_DQS_ADV_B_15: track 0.00 -> 11.6 mm
- net IO_L21P_T3_DQS_15: track 0.00 -> 11.6 mm
- net IO_L24N_T3_RS0_15: track 0.00 -> 11.6 mm
- net IO_L21N_T3_DQS_A18_15: track 0.00 -> 11.6 mm
- net IO_L18P_T2_A24_15: track 0.00 -> 11.6 mm
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- added copper zone on In2.Cu, net +1V0
- added copper zone on In2.Cu, net +1V8

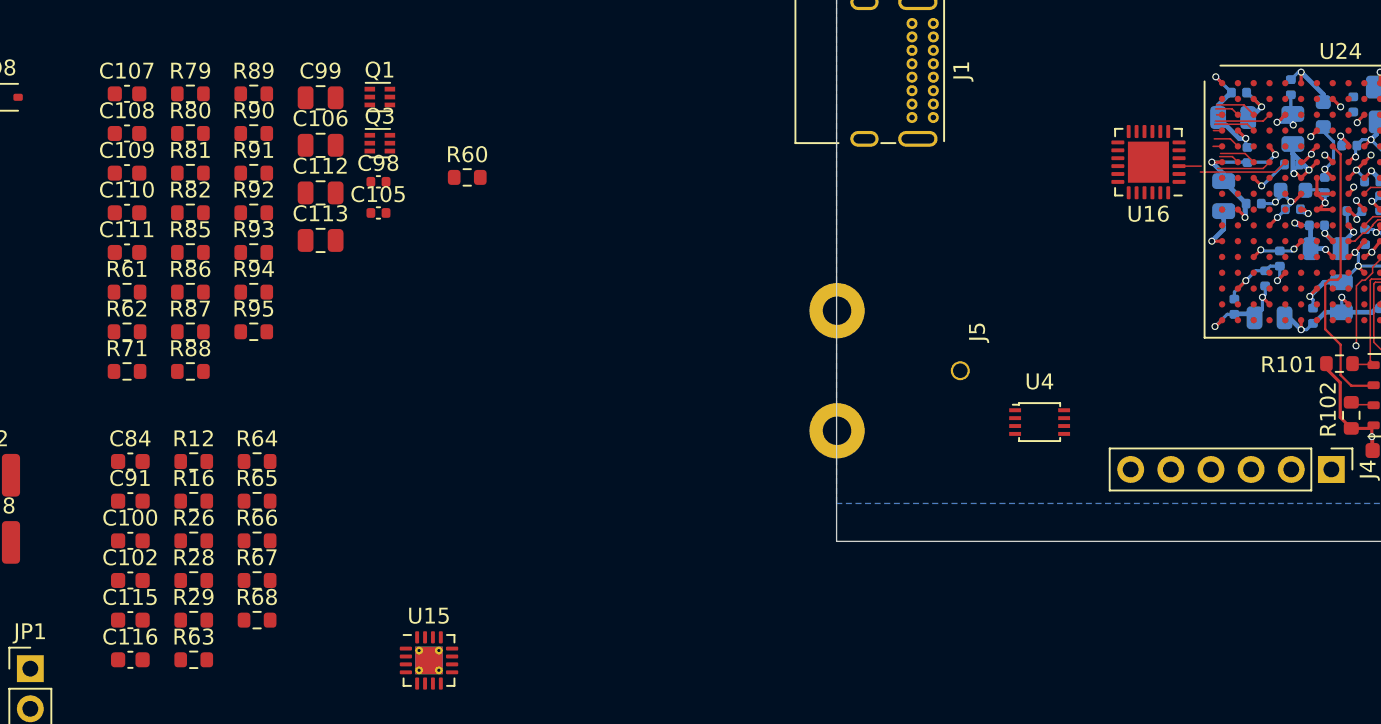
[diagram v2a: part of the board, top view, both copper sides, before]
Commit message: connected ulpi PHY
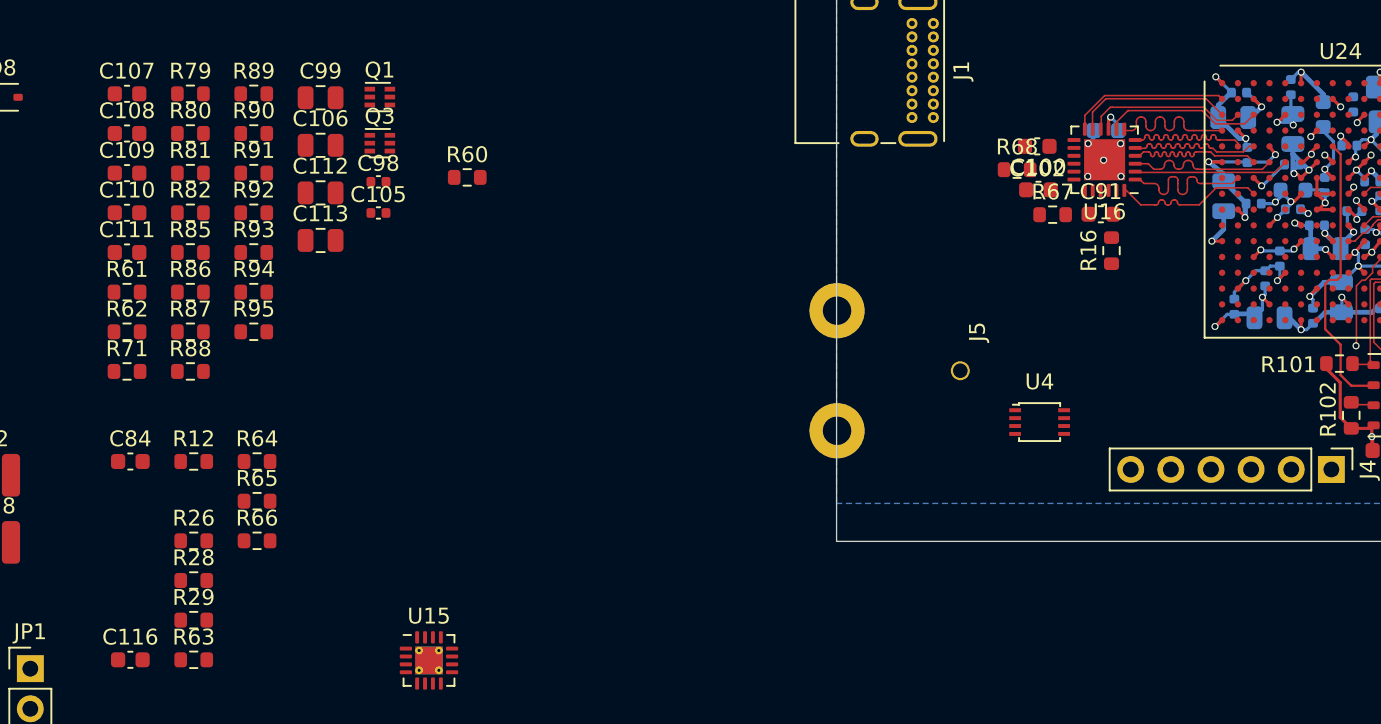
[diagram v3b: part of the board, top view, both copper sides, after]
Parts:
- C115: moved to B.Cu
- moved C115 69.1 mm to (80.0, 57.0)
- moved C91 64.0 mm to (79.7, 62.3)
- moved C102 63.6 mm to (75.7, 58.0), turned to 180 degrees
- moved C100 61.6 mm to (75.8, 60.8)
- moved R16 60.2 mm to (80.4, 64.6), turned to 90 degrees
- moved R68 55.9 mm to (74.4, 59.5)
- moved R67 55.4 mm to (76.7, 62.3)
- moved U16 2.78 mm to (80.0, 58.9)
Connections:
- Q4 pad 5: IO_L21N_T3_DQS_35 -> /Front End/PGA_SDAT
- R16 pad 2: IO_L19P_T3_A10_D26_14 -> /USB/ULPI_RSTb
- U16 pad 1: IO_L14P_T2_SRCC_14 -> IO_L17P_T2_35
- U16 pad 10: IO_L17N_T2_A13_D29_14 -> IO_L7N_T1_AD6N_35
- U16 pad 11: IO_L18P_T2_A12_D28_14 -> IO_L9P_T1_DQS_AD7P_35
- U16 pad 12: IO_L18N_T2_A11_D27_14 -> IO_L9N_T1_DQS_AD7N_35
- U16 pad 2: IO_L13P_T2_MRCC_14 -> IO_L13P_T2_MRCC_35
- U16 pad 22: IO_L19P_T3_A10_D26_14 -> /USB/ULPI_RSTb
- U16 pad 24: IO_L14N_T2_SRCC_14 -> IO_L21N_T3_DQS_35
- U16 pad 3: IO_L13N_T2_MRCC_14 -> IO_L14P_T2_SRCC_35
- U16 pad 4: IO_L15P_T2_DQS_RDWR_B_14 -> IO_L14N_T2_SRCC_35
- U16 pad 5: IO_L15N_T2_DQS_DOUT_CSO_B_14 -> IO_L11P_T1_SRCC_35
- U16 pad 6: IO_L16P_T2_CSI_B_14 -> IO_L10P_T1_AD15P_35
- U16 pad 7: IO_L16N_T2_A15_D31_14 -> IO_L10N_T1_AD15N_35
- U16 pad 8: IO_L17P_T2_A14_D30_14 -> IO_L7P_T1_AD6P_35
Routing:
- net IO_L9N_T1_DQS_AD7N_35: track 0.00 -> 9.81 mm
- net IO_L21N_T3_DQS_35: track 0.00 -> 9.70 mm
- net IO_L17P_T2_35: track 0.00 -> 9.65 mm
- net IO_L11P_T1_SRCC_35: track 0.00 -> 9.59 mm
- net IO_L9P_T1_DQS_AD7P_35: track 0.35 -> 9.66 mm
- net IO_L10N_T1_AD15N_35: track 0.55 -> 9.61 mm
- net IO_L7N_T1_AD6N_35: track 1.56 -> 9.82 mm
- net IO_L10P_T1_AD15P_35: track 1.70 -> 9.56 mm
- net IO_L14N_T2_SRCC_35: track 2.33 -> 9.63 mm
- net IO_L7P_T1_AD6P_35: track 2.61 -> 9.66 mm
- net IO_L14P_T2_SRCC_35: track 3.44 -> 9.66 mm
- net IO_L13P_T2_MRCC_35: track 5.63 -> 9.42 mm
- net IO_L12N_T1_MRCC_35: track 3.59 -> 0.00 mm
- net IO_L11N_T1_SRCC_35: track 2.64 -> 0.00 mm
- net +1V8: track 85.7 -> 88.1 mm, vias 28 -> 29
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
